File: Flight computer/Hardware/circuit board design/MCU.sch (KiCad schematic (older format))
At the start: 30 parts, among them J1 Conn_01x04, J5 USB_B_Micro, U11 ATSAML21J18B-MUT, U7 W74M64FV, Y2 32.768KHz, Y3 16MHz

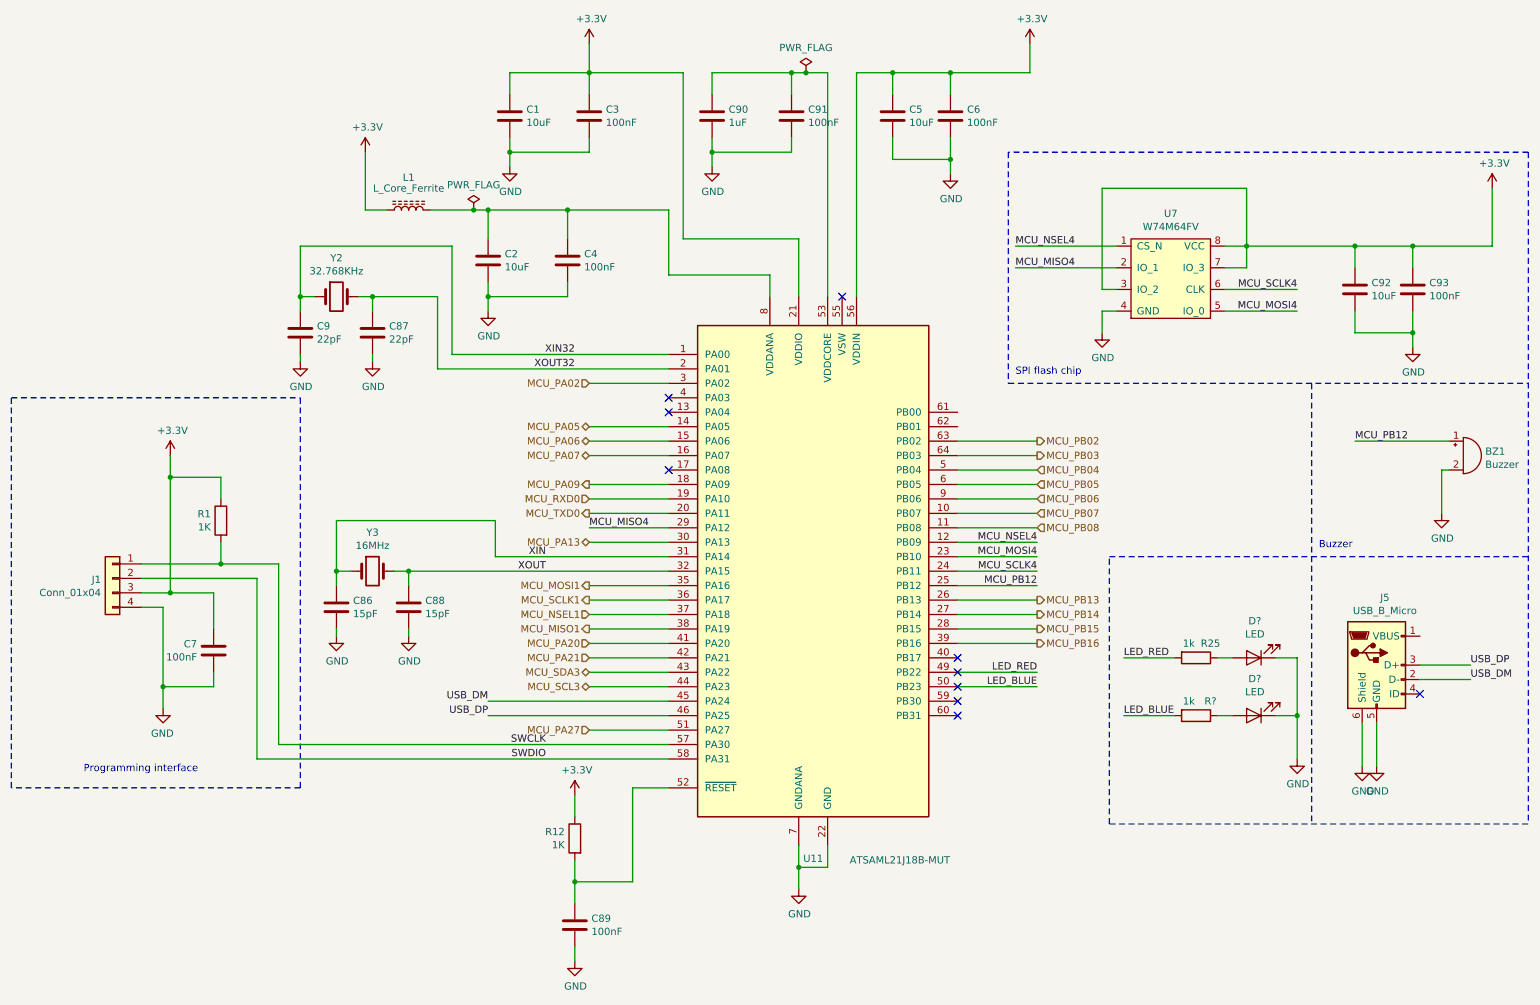
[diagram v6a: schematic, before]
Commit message: moved the USB connector to power_supply schematic
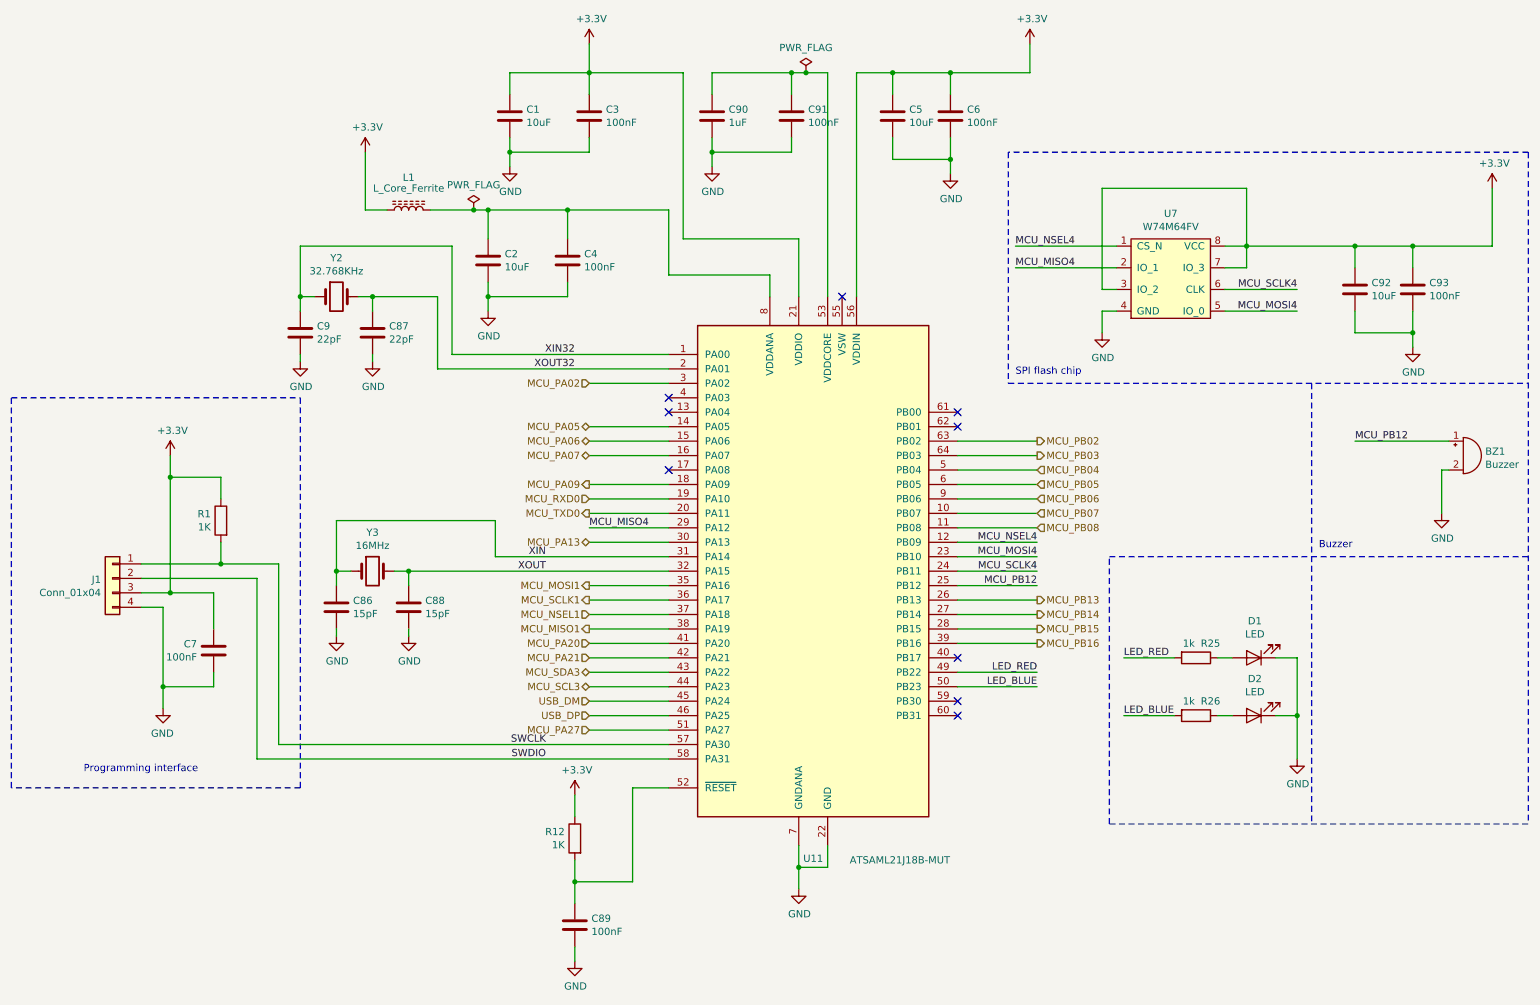
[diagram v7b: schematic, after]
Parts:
- removed J5: USB_B_Micro, Connector_USB:USB_Micro-B_Molex-105017-0001, symbol Connector:USB_B_Micro
- gave numbers to parts that had none: 3
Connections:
- no-connect marks 10 -> 9
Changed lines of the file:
@@
 Text Label 4250 5700 2    50   ~ 0
 SWDIO
-Text Label 3850 5300 2    50   ~ 0
-USB_DM
-Text Label 3850 5400 2    50   ~ 0
-USB_DP
-Wire Wire Line
-	3850 5300 5100 5300
-Wire Wire Line
-	3850 5400 5100 5400
 $Comp
 L power:GND #PWR089
@@
 NoConn ~ 7100 5400
 NoConn ~ 7100 5300
-NoConn ~ 7100 5200
-NoConn ~ 7100 5100
 NoConn ~ 7100 5000
 Wire Notes Line
@@
 Text Notes 7500 3050 0    50   ~ 0
 SPI flash chip
-Text Label 10650 5150 0    50   ~ 0
-USB_DM
-Text Label 10650 5050 0    50   ~ 0
-USB_DP
 Text HLabel 7650 3600 2    50   Output ~ 0
 MCU_PB03
@@
 Wire Wire Line
 	7650 4400 7100 4400
-NoConn ~ 10300 5250
-Wire Wire Line
-	9900 5450 9900 5750
-$Comp
-L power:GND #PWR0104
-U 1 1 5D7F3C59
-P 9900 5750
-F 0 "#PWR0104" H 9900 5500 50  0001 C CNN
-F 1 "GND" H 9905 5577 50  0000 C CNN
-F 2 "" H 9900 5750 50  0001 C CNN
-F 3 "" H 9900 5750 50  0001 C CNN
-	1    9900 5750
-	1    0    0    -1
-$EndComp
-Wire Wire Line
-	10000 5450 10000 5750
-Wire Wire Line
-	10650 5050 10300 5050
-Wire Wire Line
-	10300 5150 10650 5150
-$Comp
-L power:GND #PWR0103
-U 1 1 5D7AB0A9
-P 10000 5750
-F 0 "#PWR0103" H 10000 5500 50  0001 C CNN
-F 1 "GND" H 10005 5577 50  0000 C CNN
-F 2 "" H 10000 5750 50  0001 C CNN
-F 3 "" H 10000 5750 50  0001 C CNN
-	1    10000 5750
-	1    0    0    -1
-$EndComp
 Wire Wire Line
 	7650 4500 7100 4500
@@
 	0    1    1    0
 $EndComp
-$Comp
-L Connector:USB_B_Micro J5
-U 1 1 5D7395BE
-P 10000 5050
-F 0 "J5" H 10057 5517 50  0000 C CNN
-F 1 "USB_B_Micro" H 10057 5426 50  0000 C CNN
-F 2 "Connector_USB:USB_Micro-B_Molex-105017-0001" H 10150 5000 50  0001 C CNN
-F 3 "~" H 10150 5000 50  0001 C CNN
-	1    10000 5050
-	1    0    0    -1
-$EndComp
 Wire Notes Line
 	11050 1500 11050 6150
@@
 	9300 5000 9450 5000
 $Comp
-L Device:LED D?
+L Device:LED D1
 U 1 1 5D84CD91
 P 9150 5000
-F 0 "D?" H 9143 4745 50  0000 C CNN
+F 0 "D1" H 9143 4745 50  0000 C CNN
 F 1 "LED" H 9143 4836 50  0000 C CNN
 F 2 "" H 9150 5000 50  0001 C CNN
@@
 	8900 5000 9000 5000
 $Comp
-L Device:R R?
+L Device:R R26
 U 1 1 5D8A257E
 P 8750 5400
-F 0 "R?" V 8650 5500 50  0000 C CNN
+F 0 "R26" V 8650 5500 50  0000 C CNN
 F 1 "1k" V 8650 5350 50  0000 C CNN
 F 2 "" V 8680 5400 50  0001 C CNN
@@
 	9300 5400 9450 5400
 $Comp
-L Device:LED D?
+L Device:LED D2
 U 1 1 5D8A258A
 P 9150 5400
-F 0 "D?" H 9143 5145 50  0000 C CNN
+F 0 "D2" H 9143 5145 50  0000 C CNN
 F 1 "LED" H 9143 5236 50  0000 C CNN
 F 2 "" H 9150 5400 50  0001 C CNN
@@
 	7100 5200 7650 5200
 $Comp
-L power:GND #PWR?
+L power:GND #PWR0106
 U 1 1 5D8CC1E1
 P 9450 5700
-F 0 "#PWR?" H 9450 5450 50  0001 C CNN
+F 0 "#PWR0106" H 9450 5450 50  0001 C CNN
 F 1 "GND" H 9455 5527 50  0000 C CNN
 F 2 "" H 9450 5700 50  0001 C CNN
@@
 Wire Wire Line
 	8600 5000 8250 5000
+NoConn ~ 7100 3400
+NoConn ~ 7100 3300
+Text HLabel 4550 5400 0    50   Input ~ 0
+USB_DP
+Text HLabel 4550 5300 0    50   Input ~ 0
+USB_DM
+Wire Wire Line
+	4550 5400 5100 5400
+Wire Wire Line
+	4550 5300 5100 5300
 $EndSCHEMATC

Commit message: removed the 37khz crystal
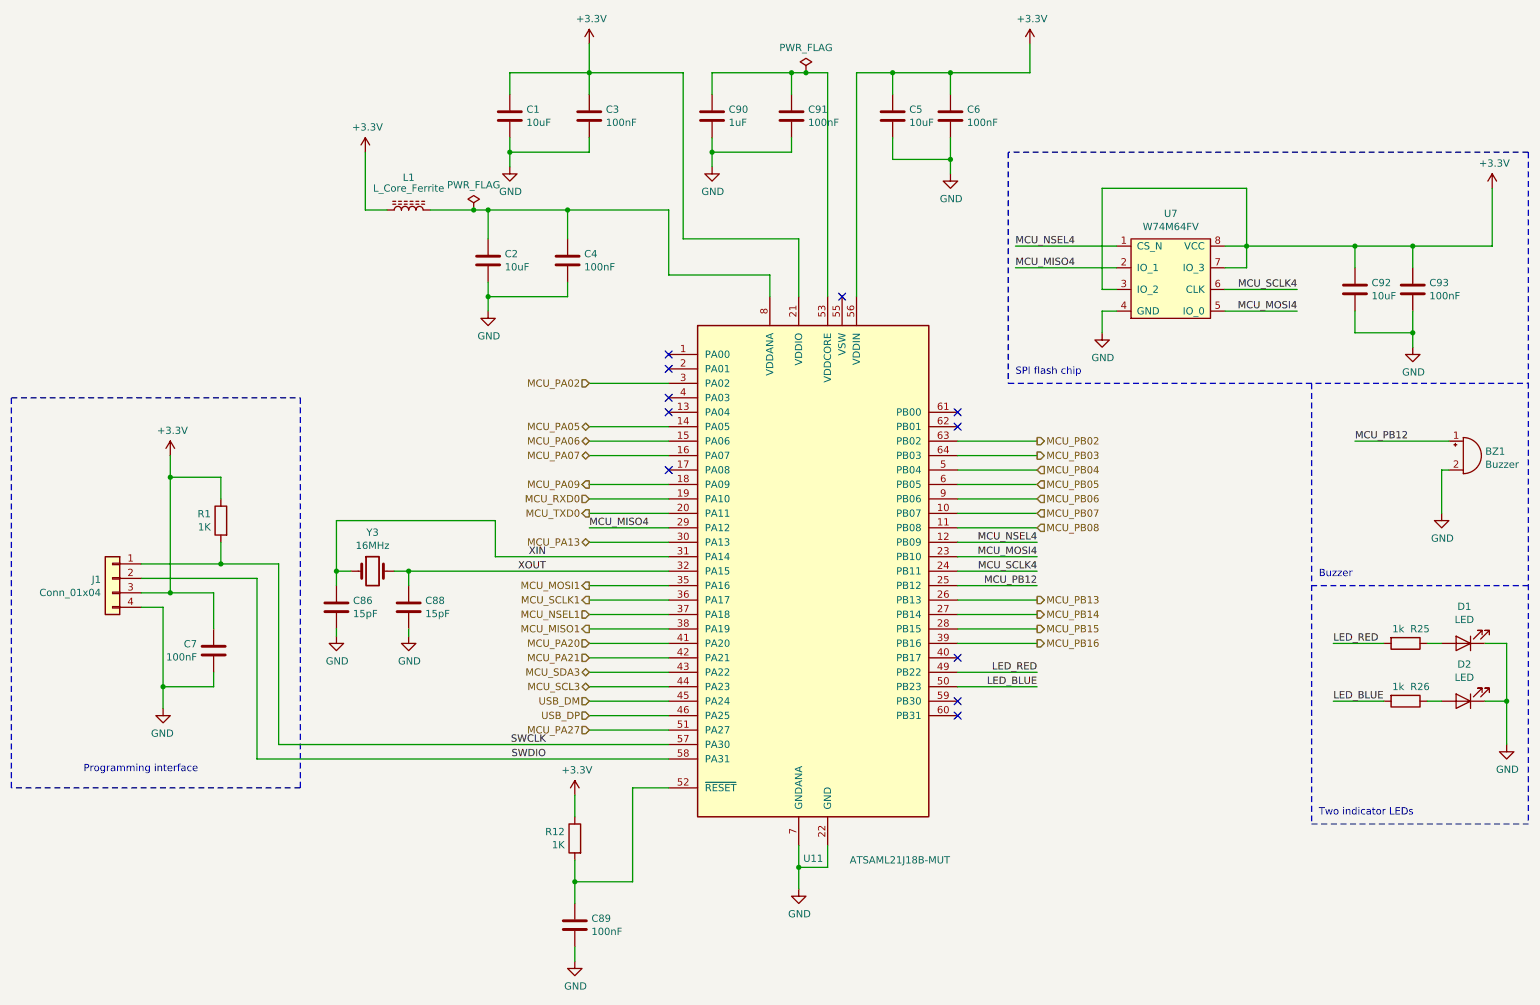
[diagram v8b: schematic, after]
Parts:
- removed C87, C9: 22pF, Capacitor_SMD:C_0402_1005Metric, symbol Device:C
- removed Y2: 32.768KHz, Crystal:Crystal_SMD_2012-2Pin_2.0x1.2mm, symbol Device:Crystal
- D1, D2: footprint (none) -> LED_SMD:LED_0603_1608Metric
- R25, R26: footprint (none) -> Resistor_SMD:R_0603_1608Metric
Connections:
- net XIN32: no longer names the net of U11.1 (PA00)
- net XOUT32: no longer names the net of U11.2 (PA01)
- no-connect marks 9 -> 11
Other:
- note added: "Two indicator LEDs"
- moved on the sheet: D1, D2, R25, R26
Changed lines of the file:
@@
 Wire Wire Line
 	6000 6450 6000 6300
-Text Label 4450 2900 2    50   ~ 0
-XIN32
-Text Label 4450 3000 2    50   ~ 0
-XOUT32
 Text Label 4250 4300 2    50   ~ 0
 XIN
@@
 Wire Wire Line
 	2250 4450 1450 4450
-$Comp
-L Device:Crystal Y2
-U 1 1 5D6CAE6E
-P 2800 2500
-F 0 "Y2" H 2800 2768 50  0000 C CNN
-F 1 "32.768KHz" H 2800 2677 50  0000 C CNN
-F 2 "Crystal:Crystal_SMD_2012-2Pin_2.0x1.2mm" H 2800 2500 50  0001 C CNN
-F 3 "~" H 2800 2500 50  0001 C CNN
-	1    2800 2500
-	1    0    0    -1
-$EndComp
-$Comp
-L Device:C C87
-U 1 1 5D6CBAAC
-P 3050 2750
-F 0 "C87" H 3165 2796 50  0000 L CNN
-F 1 "22pF" H 3165 2705 50  0000 L CNN
-F 2 "Capacitor_SMD:C_0402_1005Metric" H 3088 2600 50  0001 C CNN
-F 3 "~" H 3050 2750 50  0001 C CNN
-	1    3050 2750
-	1    0    0    -1
-$EndComp
-$Comp
-L Device:C C9
-U 1 1 5D6CC221
-P 2550 2750
-F 0 "C9" H 2665 2796 50  0000 L CNN
-F 1 "22pF" H 2665 2705 50  0000 L CNN
-F 2 "Capacitor_SMD:C_0402_1005Metric" H 2588 2600 50  0001 C CNN
-F 3 "~" H 2550 2750 50  0001 C CNN
-	1    2550 2750
-	1    0    0    -1
-$EndComp
-$Comp
-L power:GND #PWR04
-U 1 1 5D6CF38C
-P 2550 2950
-F 0 "#PWR04" H 2550 2700 50  0001 C CNN
-F 1 "GND" H 2555 2777 50  0000 C CNN
-F 2 "" H 2550 2950 50  0001 C CNN
-F 3 "" H 2550 2950 50  0001 C CNN
-	1    2550 2950
-	1    0    0    -1
-$EndComp
-$Comp
-L power:GND #PWR084
-U 1 1 5D6D2421
-P 3050 2950
-F 0 "#PWR084" H 3050 2700 50  0001 C CNN
-F 1 "GND" H 3055 2777 50  0000 C CNN
-F 2 "" H 3050 2950 50  0001 C CNN
-F 3 "" H 3050 2950 50  0001 C CNN
-	1    3050 2950
-	1    0    0    -1
-$EndComp
-Wire Wire Line
-	3050 2600 3050 2500
-Connection ~ 3050 2500
-Wire Wire Line
-	3050 2500 2950 2500
-Wire Wire Line
-	2650 2500 2550 2500
-Wire Wire Line
-	2550 2500 2550 2600
-Wire Wire Line
-	2550 2950 2550 2900
-Wire Wire Line
-	3050 2950 3050 2900
-Wire Wire Line
-	2550 2500 2550 2150
-Wire Wire Line
-	2550 2150 3600 2150
-Wire Wire Line
-	3600 2150 3600 2900
-Wire Wire Line
-	3600 2900 5100 2900
-Connection ~ 2550 2500
-Wire Wire Line
-	3500 3000 3500 2500
-Wire Wire Line
-	3500 3000 5100 3000
-Wire Wire Line
-	3050 2500 3500 2500
 $Comp
 L Device:Crystal Y3
@@
 Text Label 7650 4500 2    50   ~ 0
 MCU_PB12
-Text Notes 9600 4250 0    50   ~ 0
+Text Notes 9600 4450 0    50   ~ 0
 Buzzer\n
 Wire Wire Line
@@
 NoConn ~ 5100 3300
 NoConn ~ 5100 3200
-$Comp
-L Device:R R25
-U 1 1 5D84A9D3
-P 8750 5000
-F 0 "R25" V 8650 5100 50  0000 C CNN
-F 1 "1k" V 8650 4950 50  0000 C CNN
-F 2 "" V 8680 5000 50  0001 C CNN
-F 3 "~" H 8750 5000 50  0001 C CNN
-	1    8750 5000
-	0    1    1    0
-$EndComp
 Wire Notes Line
 	11050 1500 11050 6150
-Wire Notes Line
-	9550 3100 9550 6150
-Wire Notes Line
-	8150 6150 8150 4300
-Wire Wire Line
-	9300 5000 9450 5000
-$Comp
-L Device:LED D1
-U 1 1 5D84CD91
-P 9150 5000
-F 0 "D1" H 9143 4745 50  0000 C CNN
-F 1 "LED" H 9143 4836 50  0000 C CNN
-F 2 "" H 9150 5000 50  0001 C CNN
-F 3 "~" H 9150 5000 50  0001 C CNN
-	1    9150 5000
-	-1   0    0    1
-$EndComp
-Wire Wire Line
-	8900 5000 9000 5000
-$Comp
-L Device:R R26
-U 1 1 5D8A257E
-P 8750 5400
-F 0 "R26" V 8650 5500 50  0000 C CNN
-F 1 "1k" V 8650 5350 50  0000 C CNN
-F 2 "" V 8680 5400 50  0001 C CNN
-F 3 "~" H 8750 5400 50  0001 C CNN
-	1    8750 5400
-	0    1    1    0
-$EndComp
-Wire Wire Line
-	9300 5400 9450 5400
-$Comp
-L Device:LED D2
-U 1 1 5D8A258A
-P 9150 5400
-F 0 "D2" H 9143 5145 50  0000 C CNN
-F 1 "LED" H 9143 5236 50  0000 C CNN
-F 2 "" H 9150 5400 50  0001 C CNN
-F 3 "~" H 9150 5400 50  0001 C CNN
-	1    9150 5400
-	-1   0    0    1
-$EndComp
-Wire Wire Line
-	8900 5400 9000 5400
-Wire Wire Line
-	9450 5000 9450 5400
-Connection ~ 9450 5400
-Wire Wire Line
-	9450 5400 9450 5700
 Text Label 7650 5100 2    50   ~ 0
 LED_RED
@@
 L power:GND #PWR0106
 U 1 1 5D8CC1E1
-P 9450 5700
-F 0 "#PWR0106" H 9450 5450 50  0001 C CNN
-F 1 "GND" H 9455 5527 50  0000 C CNN
-F 2 "" H 9450 5700 50  0001 C CNN
-F 3 "" H 9450 5700 50  0001 C CNN
-	1    9450 5700
-	1    0    0    -1
-$EndComp
-Text Label 8250 5000 0    50   ~ 0
-LED_RED
-Text Label 8250 5400 0    50   ~ 0
-LED_BLUE
-Wire Notes Line
-	8150 6150 11050 6150
-Wire Notes Line
-	8150 4300 11050 4300
-Wire Wire Line
-	8600 5400 8250 5400
-Wire Wire Line
-	8600 5000 8250 5000
+P 10900 5600
+F 0 "#PWR0106" H 10900 5350 50  0001 C CNN
+F 1 "GND" H 10905 5427 50  0000 C CNN
+F 2 "" H 10900 5600 50  0001 C CNN
+F 3 "" H 10900 5600 50  0001 C CNN
+	1    10900 5600
+	1    0    0    -1
+$EndComp
 NoConn ~ 7100 3400
 NoConn ~ 7100 3300
@@
 Wire Wire Line
 	4550 5300 5100 5300
+Wire Wire Line
+	10900 5300 10900 5600
+Connection ~ 10900 5300
+Wire Wire Line
+	10900 4900 10900 5300
+Wire Wire Line
+	10050 4900 9700 4900
+Wire Wire Line
+	10050 5300 9700 5300
+Text Label 9700 5300 0    50   ~ 0
+LED_BLUE
+Text Label 9700 4900 0    50   ~ 0
+LED_RED
+Wire Wire Line
+	10350 5300 10450 5300
+$Comp
+L Device:LED D2
+U 1 1 5D8A258A
+P 10600 5300
+F 0 "D2" H 10593 5045 50  0000 C CNN
+F 1 "LED" H 10593 5136 50  0000 C CNN
+F 2 "LED_SMD:LED_0603_1608Metric" H 10600 5300 50  0001 C CNN
+F 3 "~" H 10600 5300 50  0001 C CNN
+	1    10600 5300
+	-1   0    0    1
+$EndComp
+Wire Wire Line
+	10750 5300 10900 5300
+$Comp
+L Device:R R26
+U 1 1 5D8A257E
+P 10200 5300
+F 0 "R26" V 10100 5400 50  0000 C CNN
+F 1 "1k" V 10100 5250 50  0000 C CNN
+F 2 "Resistor_SMD:R_0603_1608Metric" V 10130 5300 50  0001 C CNN
+F 3 "~" H 10200 5300 50  0001 C CNN
+	1    10200 5300
+	0    1    1    0
+$EndComp
+Wire Wire Line
+	10350 4900 10450 4900
+$Comp
+L Device:LED D1
+U 1 1 5D84CD91
+P 10600 4900
+F 0 "D1" H 10593 4645 50  0000 C CNN
+F 1 "LED" H 10593 4736 50  0000 C CNN
+F 2 "LED_SMD:LED_0603_1608Metric" H 10600 4900 50  0001 C CNN
+F 3 "~" H 10600 4900 50  0001 C CNN
+	1    10600 4900
+	-1   0    0    1
+$EndComp
+Wire Wire Line
+	10750 4900 10900 4900
+$Comp
+L Device:R R25
+U 1 1 5D84A9D3
+P 10200 4900
+F 0 "R25" V 10100 5000 50  0000 C CNN
+F 1 "1k" V 10100 4850 50  0000 C CNN
+F 2 "Resistor_SMD:R_0603_1608Metric" V 10130 4900 50  0001 C CNN
+F 3 "~" H 10200 4900 50  0001 C CNN
+	1    10200 4900
+	0    1    1    0
+$EndComp
+Wire Notes Line
+	9550 6150 11050 6150
+Wire Notes Line
+	9550 3100 9550 6150
+Wire Notes Line
+	11050 4500 9550 4500
+Text Notes 9600 6100 0    50   ~ 0
+Two indicator LEDs
+NoConn ~ 5100 3000
+NoConn ~ 5100 2900
 $EndSCHEMATC
